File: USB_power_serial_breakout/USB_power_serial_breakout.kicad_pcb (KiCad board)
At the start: 2 copper layers, 53.3 x 26.7 mm, 23 parts, among them J1 Mount2, J2 Mount2, J3 USB_B, J4 UART, U1 FT230XS

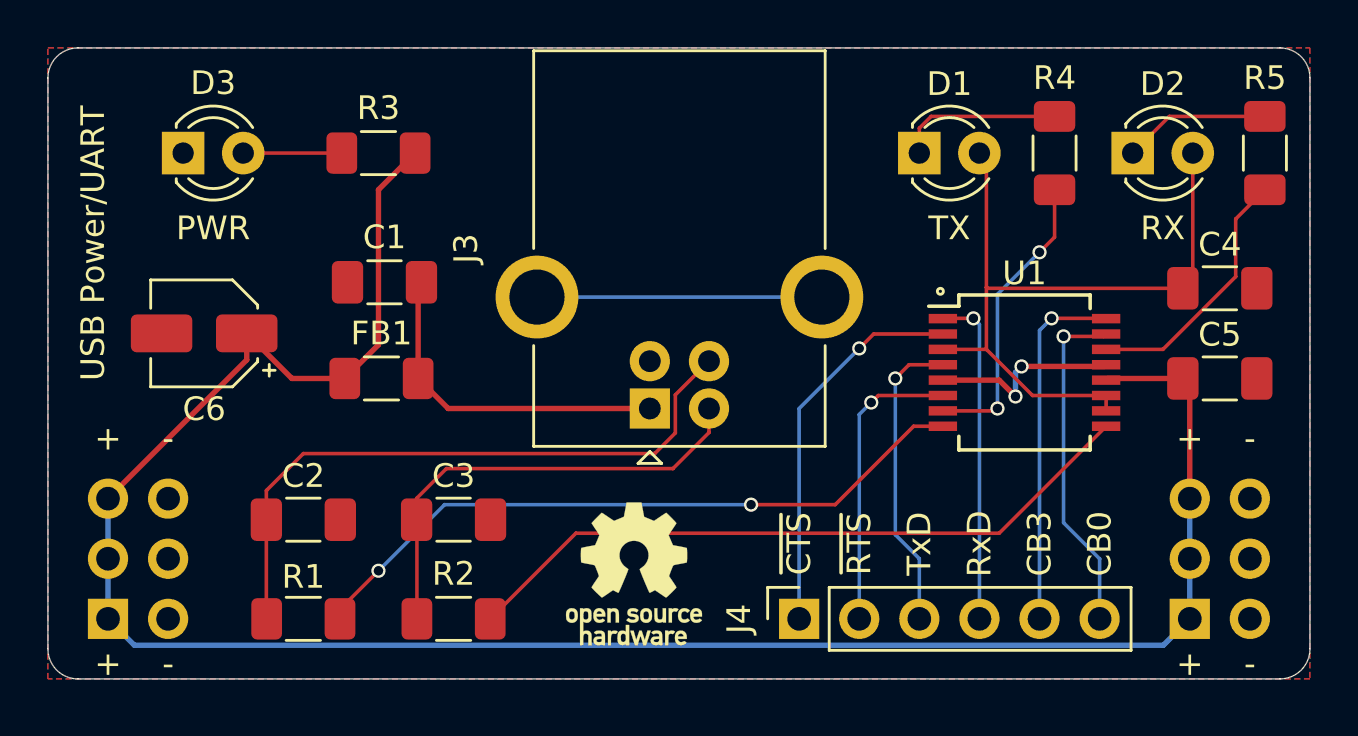
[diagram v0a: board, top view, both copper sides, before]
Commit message: Updated USB/UART board
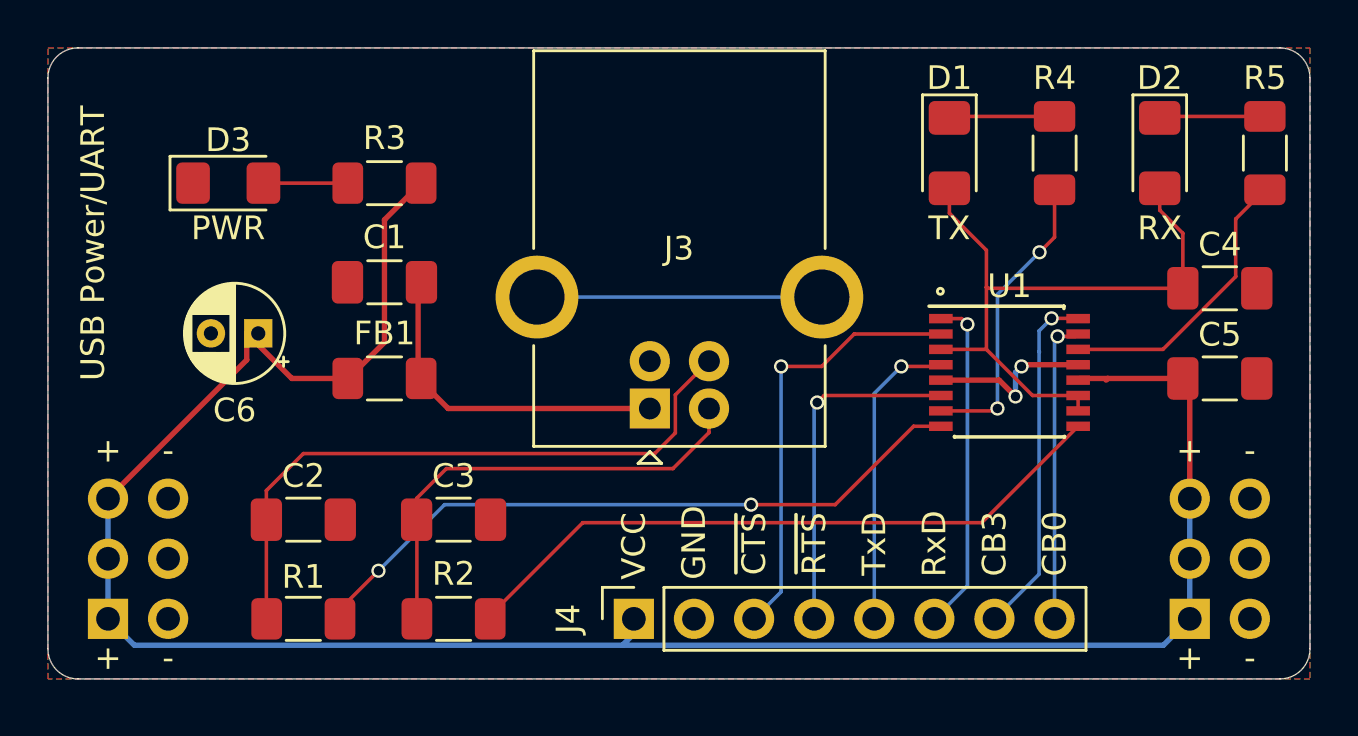
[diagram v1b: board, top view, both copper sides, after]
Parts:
- C6: footprint Capacitor_SMD:CP_Elec_4x5.8 -> Capacitor_THT:CP_Radial_D4.0mm_P2.00mm
- D1, D2, D3: footprint LED_THT:LED_D3.0mm -> LED_SMD:LED_1206_3216Metric_Pad1.42x1.75mm_HandSolder
- J4: footprint Connector_PinSocket_2.54mm:PinSocket_1x06_P2.54mm_Vertical -> Connector_PinSocket_2.54mm:PinSocket_1x08_P2.54mm_Vertical
- REF**: moved to B.Cu
- U1: footprint Package_SO:SSOP-16_5.3x6.2mm_P0.65mm -> Package_SO:SSOP-16_4.4x5.2mm_P0.65mm
- moved REF** 13.5 mm to (217.2, 71.1), turned to 180 degrees
- moved J4 6.99 mm to (215.3, 86.4)
- moved D3 2.29 mm to (198.1, 67.9)
- moved C6 2.29 mm to (199.4, 74.3)
- moved R3 1.30 mm to (204.7, 67.9)
- moved D1 1.27 mm to (228.6, 66.7), turned to 270 degrees
- moved D2 1.14 mm to (237.5, 66.7), turned to 270 degrees
- moved U1 0.64 mm to (231.1, 75.9)
- moved FB1 0.13 mm to (204.7, 76.2)
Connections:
- J4 pad 1: ~RTS -> VCC
- J4 pad 2: ~CTS -> GND
- J4 pad 3: RxD -> ~RTS
- J4 pad 4: TxD -> ~CTS
- J4 pad 5: CBUS3 -> RxD
- J4 pad 6: CBUS0 -> TxD
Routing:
- net Net-(C4-Pad1): track 31.0 -> 28.2 mm
- net Net-(D2-Pad1): track 6.23 -> 4.04 mm
- net ~RTS: track 16.3 -> 18.5 mm
- net ~CTS: track 12.5 -> 14.5 mm
- net Net-(D1-Pad1): track 6.97 -> 5.22 mm
- net CBUS0: track 14.4 -> 12.9 mm
- net VCC: track 90.4 -> 91.8 mm
- net GND: track 8.34 -> 7.15 mm
- net ~RXLED: track 10.9 -> 12.1 mm
- net USBD-: track 29.4 -> 28.3 mm
- net Net-(D3-Pad2): track 4.16 -> 3.57 mm
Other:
- board text added: "GND"
- board text added: "VCC"
- board text added: "Version 2"
- board text removed: "Version 1"

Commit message: PCB RC2
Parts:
- moved QR***** 5.12 mm to (197.5, 69.2)
- moved REF** 4.62 mm to (235.6, 69.2)
- moved D1 2.01 mm to (226.7, 67.3)
- moved D2 2.01 mm to (235.6, 67.3)
- moved R4 2.01 mm to (231.1, 67.3)
- moved R5 2.01 mm to (240.0, 67.3)
- moved C6 1.91 mm to (199.4, 76.2)
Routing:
- net VCC: track 91.8 -> 89.5 mm
- net ~TXLED: track 12.6 -> 11.2 mm
- net ~RXLED: track 12.1 -> 10.7 mm
- net Net-(D1-Pad1): track 5.22 -> 4.47 mm
